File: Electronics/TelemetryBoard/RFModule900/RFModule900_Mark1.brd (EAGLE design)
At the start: 100 x 30 mm, 166 parts, among them T1 DC08-73, T2 DC08-73, U1 TPS2561, U2 TPS2561, U3 LM75B, U4 LTC5505, U5 LTC5505, U6 MCP4728, U7 ADC128D818, U8 MIC5504-3.3YM5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

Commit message: Working on routing board
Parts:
- moved D13 96.1 mm to (5.08, 8.89), turned to 180 degrees
- moved U$20 82.5 mm to (20.3, 5.08), flipped to the bottom
- moved R40 79.0 mm to (24.1, 5.08), flipped to the bottom
- moved C59 75.7 mm to (6.03, 3.81), turned to 270 degrees
- moved D10 74.0 mm to (5.08, 15.2), turned to 180 degrees
- moved R25 70.9 mm to (34.3, 8.89)
- moved R26 70.9 mm to (34.3, 5.08)
- moved R27 70.9 mm to (34.3, 12.7)
- moved C47 70.5 mm to (80.0, 5.08)
- moved R30 69.7 mm to (29.2, 10.2)
- moved D11 68.3 mm to (5.08, 25.4), turned to 0 degrees
- moved C58 67.1 mm to (10.2, 3.81), turned to 270 degrees
- moved C60 67.0 mm to (14.3, 10.8)
- moved D7 65.5 mm to (5.08, 22.9), turned to 0 degrees
- moved C46 65.0 mm to (82.5, 6.35)
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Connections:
- net TR_SWITCH_CTL: now also U$11.2
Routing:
- added copper zone on layer 1, net GND
- added copper zone on layer 15, net GND
- added copper zone on layer 16, net GND
- added copper zone on layer 2, net GND
- removed copper zone on layer 16, net N$3

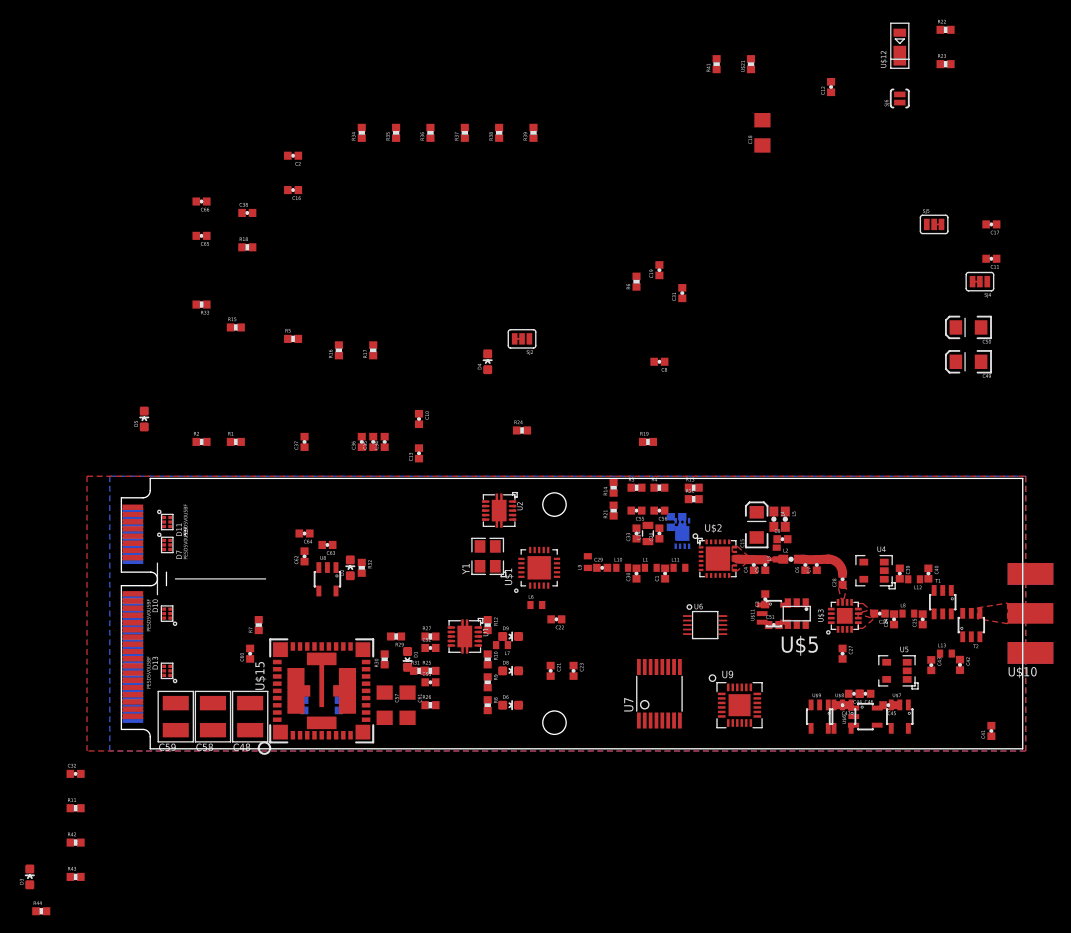
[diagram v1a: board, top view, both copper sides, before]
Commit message: Routing analog sections
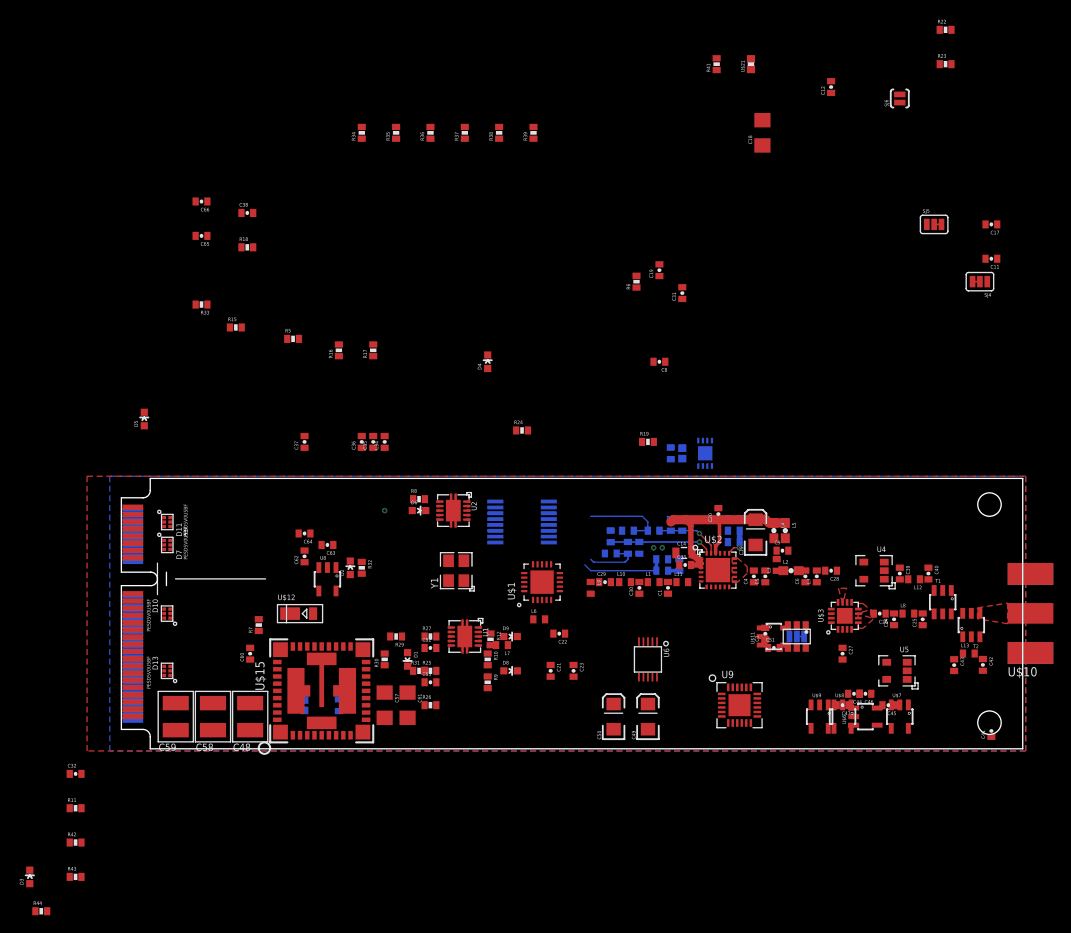
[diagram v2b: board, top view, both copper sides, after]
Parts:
- moved U$12 91.6 mm to (20.3, 15.2), turned to 0 degrees
- moved C16 61.0 mm to (67.9, 25.7), flipped to the bottom
- moved C2 60.7 mm to (60.0, 21.3), flipped to the bottom
- moved C50 58.4 mm to (54.6, 3.81), turned to 90 degrees
- moved R1 56.1 mm to (67.9, 24.4), flipped to the bottom, turned to 180 degrees
- moved R2 53.1 mm to (60.0, 20.0), flipped to the bottom, turned to 180 degrees
- moved C49 53.1 mm to (58.4, 3.81), turned to 90 degrees
- moved SJ2 44.9 mm to (74.9, 12.7), flipped to the bottom
- moved C10 37.5 mm to (67.9, 23.2), flipped to the bottom, turned to 180 degrees
- moved C13 31.4 mm to (61.9, 20.6), flipped to the bottom, turned to 270 degrees
- moved U7 24.4 mm to (44.5, 25.4), flipped to the bottom, turned to 90 degrees
- moved R8 24.1 mm to (33.0, 27.9), turned to 0 degrees
- moved D6 23.9 mm to (33.0, 26.7)
- moved U3 9.25 mm to (64.8, 33.0)
- moved R20 9.08 mm to (56.2, 22.5), flipped to the bottom, turned to 270 degrees
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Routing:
- net PA_3V6: track 0.00 -> 26.8 mm
- net N$48: track 0.00 -> 11.4 mm, vias 0 -> 1
- net VREG2_DAC: track 0.00 -> 9.46 mm
- net PA_PWR_SENSE: track 0.00 -> 9.12 mm
- net N$47: track 0.00 -> 7.31 mm, vias 0 -> 1
- net PA_PWR_REF: track 0.00 -> 6.27 mm
- net N$5: track 5.97 -> 0.00 mm
- net N$8: track 5.55 -> 0.00 mm
- net N$2: track 0.00 -> 3.37 mm, vias 0 -> 1
- net N$9: track 0.00 -> 1.26 mm

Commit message: Work in progress routing PSU
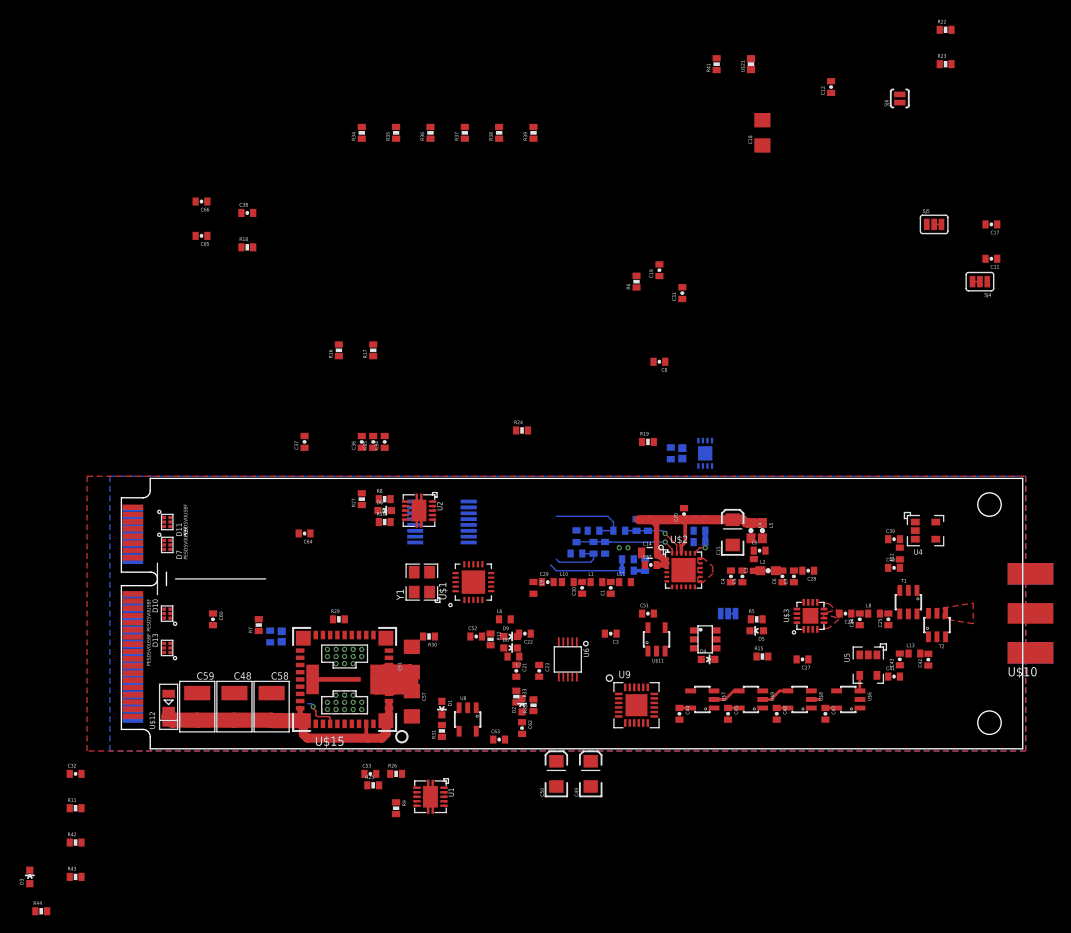
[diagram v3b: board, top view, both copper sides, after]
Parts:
- moved D5 71.9 mm to (70.5, 13.3), turned to 90 degrees
- moved R15 68.9 mm to (71.1, 10.5)
- moved R5 60.1 mm to (70.5, 14.6)
- moved R33 55.8 mm to (43.8, 6.03), turned to 270 degrees
- moved D4 41.1 mm to (65.1, 10.2), turned to 270 degrees
- moved C62 30.7 mm to (44.5, 2.54), turned to 270 degrees
- moved C63 28.8 mm to (41.9, 1.27), turned to 0 degrees
- moved D2 24.4 mm to (44.5, 5.08)
- moved R32 24.4 mm to (45.7, 5.08), turned to 90 degrees
- moved U8 22.0 mm to (38.4, 3.49)
- moved U$7 22.0 mm to (64.5, 5.71), turned to 180 degrees
- moved C44 19.5 mm to (61.9, 4.13), turned to 270 degrees
- moved R10 19.0 mm to (29.2, 25.4), turned to 0 degrees
- moved U1 18.2 mm to (34.3, -5.08)
- moved U$12 18.0 mm to (5.24, 5.40), turned to 90 degrees
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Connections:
- removed net N$38: U$8.4, U$9.1
- removed net N$46: U$7.1, U$9.4
- new net N$19: U$7.2, U$9.4
- new net N$3: U$8.4, U$9.2
- net 3V6_PWRGD: no longer U9.P$7
- net PA_BREAKER_OVERRIDE: now also U$9.1; no longer U$9.2
- net PA_PWR_EN: now also U$7.1; no longer U$7.2
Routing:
- net 3.6V: track 0.00 -> 40.4 mm
- net 12V: track 0.00 -> 33.5 mm
- net 3.3V: track 0.00 -> 4.98 mm
- net 3V6_PWRGD: track 0.00 -> 4.30 mm, vias 0 -> 1
- net N$3: track 0.00 -> 3.19 mm
- net N$19: track 0.00 -> 3.19 mm
- net RF_POWER_IN: track 0.00 -> 1.73 mm
- net VSWR_BREAKER_STATE: track 0.00 -> 0.93 mm
- net PA_3V6: track 26.8 -> 27.7 mm
- removed copper zone on layer 1, net N$24

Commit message: adding backround info about modules
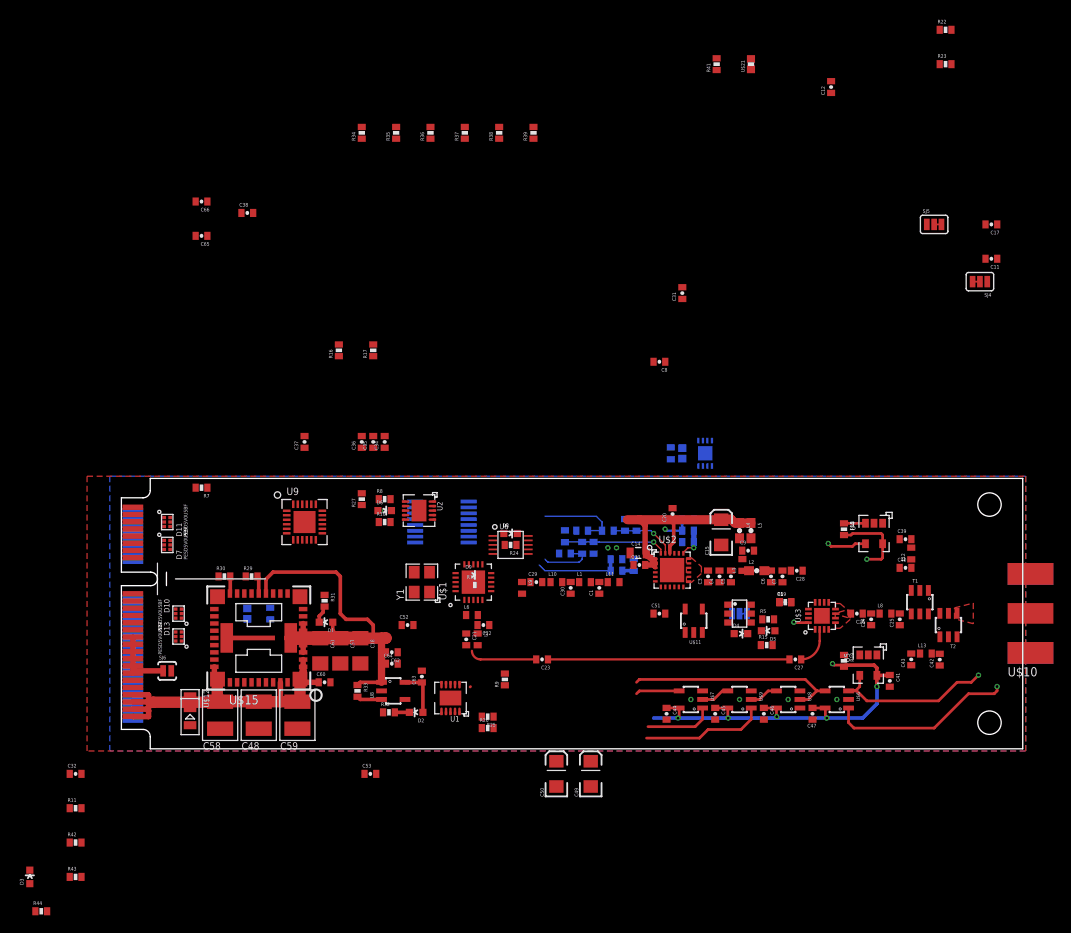
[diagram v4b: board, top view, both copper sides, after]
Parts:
- R33: value 270 -> 5k
- moved SJ6 103.1 mm to (5.08, 8.89), turned to 0 degrees
- moved R18 73.2 mm to (80.2, 24.6), turned to 270 degrees
- moved C18 72.7 mm to (26.5, 11.1), turned to 270 degrees
- moved U9 42.1 mm to (20.3, 25.4)
- moved C19 39.4 mm to (73.7, 16.5), turned to 0 degrees
- moved R6 39.2 mm to (73.7, 16.5), turned to 0 degrees
- moved R19 32.6 mm to (80.2, 10.0), turned to 270 degrees
- moved R30 23.7 mm to (11.4, 19.4), turned to 0 degrees
- moved R31 19.4 mm to (22.5, 16.7), turned to 270 degrees
- moved R9 18.7 mm to (42.5, 7.94), turned to 90 degrees
- moved R33 17.6 mm to (26.2, 6.67)
- moved C64 17.4 mm to (30.0, 9.68), turned to 0 degrees
- moved C62 16.7 mm to (30.0, 11.0), turned to 180 degrees
- moved R7 16.5 mm to (8.89, 29.2), turned to 180 degrees
- moved R32 16.1 mm to (29.7, 4.29), turned to 0 degrees
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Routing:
- net REFLECTED_POWER_REF: track 0.00 -> 91.5 mm, vias 0 -> 1
- net 3.3V: track 4.98 -> 92.4 mm, vias 0 -> 8
- net RF_POWER_IN: track 1.73 -> 84.5 mm, vias 0 -> 1
- net RF_POWER_OUT: track 0.00 -> 39.4 mm, vias 0 -> 1
- net N$14: track 0.00 -> 26.8 mm
- net VSWR_BREAKER_STATE: track 0.93 -> 23.9 mm
- net VREG1_DAC: track 0.00 -> 16.9 mm, vias 0 -> 1
- net PA_BREAKER_OVERRIDE: track 0.00 -> 13.7 mm
- net 3.6V: track 40.4 -> 53.4 mm
- net PA_PWR_EN: track 0.00 -> 7.65 mm
- net N$13: track 0.00 -> 7.52 mm
- net N$7: track 0.00 -> 7.46 mm
- net 12V: track 33.5 -> 39.6 mm
- net PA_PWR_EN_BREAKER: track 0.00 -> 4.86 mm
- net 3V6_PWRGD: track 4.30 -> 0.00 mm, vias 1 -> 0
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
